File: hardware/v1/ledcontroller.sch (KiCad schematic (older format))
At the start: 4 parts, among them U1 MAX7221

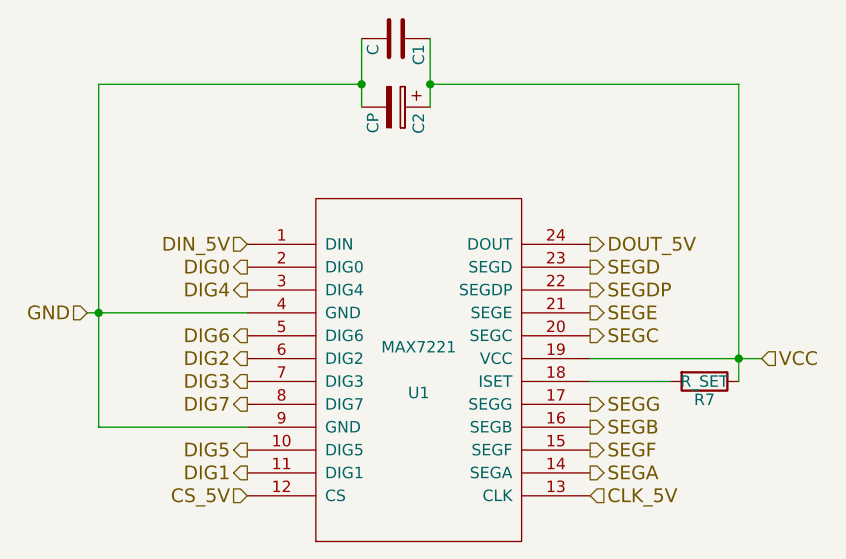
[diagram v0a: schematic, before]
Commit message: Some autorouting on 16led row
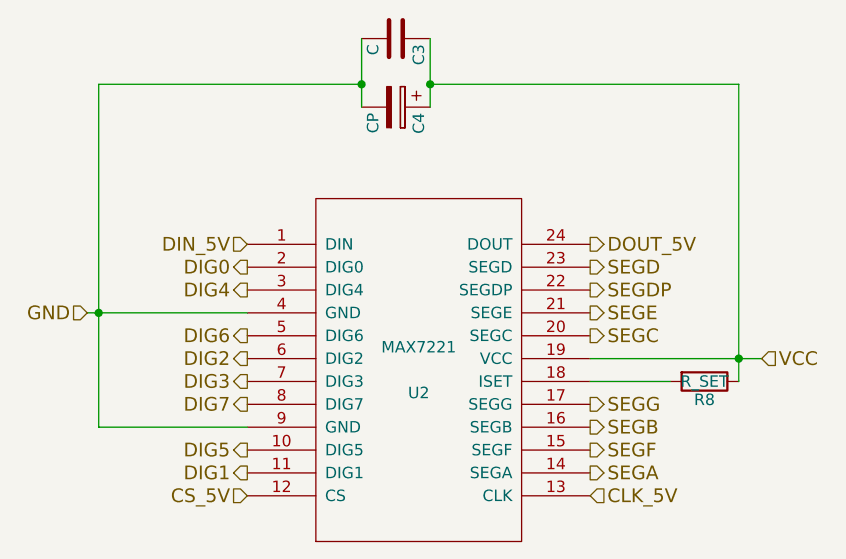
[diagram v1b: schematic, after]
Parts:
- C2: footprint Discret:CP4 -> Discret:CP36V
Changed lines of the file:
@@
 U 1 1 57A34228
 P 5750 3600
-F 0 "U1" H 5750 3500 50  0000 C CNN
+AR Path="/57A2FF40/57A5CF2B/57A34228" Ref="U1"  Part="1"
+AR Path="/57A2FF40/57A5D8B0/57A34228" Ref="U2"  Part="1"
+AR Path="/57A30207/57A34228" Ref="U4"  Part="1"
+F 0 "U2" H 5750 3500 50  0000 C CNN
 F 1 "MAX7221" H 5750 3700 50  0000 C CNN
 F 2 "DIL24:DIL24" H 5750 3600 50  0001 C CNN
@@
 U 1 1 57A343D9
 P 7000 3650
-F 0 "R7" V 7080 3650 50  0000 C CNN
+AR Path="/57A2FF40/57A5CF2B/57A343D9" Ref="R7"  Part="1"
+AR Path="/57A2FF40/57A5D8B0/57A343D9" Ref="R8"  Part="1"
+AR Path="/57A30207/57A343D9" Ref="R9"  Part="1"
+F 0 "R8" V 7080 3650 50  0000 C CNN
 F 1 "R_SET" V 7000 3650 50  0000 C CNN
 F 2 "Resistors_ThroughHole:Resistor_Horizontal_RM10mm" V 6930 3650 50  0001 C CNN
@@
 U 1 1 57A3585E
 P 5650 2150
-F 0 "C1" H 5675 2250 50  0000 L CNN
+AR Path="/57A2FF40/57A5CF2B/57A3585E" Ref="C1"  Part="1"
+AR Path="/57A2FF40/57A5D8B0/57A3585E" Ref="C3"  Part="1"
+AR Path="/57A30207/57A3585E" Ref="C5"  Part="1"
+F 0 "C3" H 5675 2250 50  0000 L CNN
 F 1 "C" H 5675 2050 50  0000 L CNN
 F 2 "Capacitors_ThroughHole:C_Disc_D6_P5" H 5688 2000 50  0001 C CNN
@@
 U 1 1 57A358C3
 P 5650 2450
-F 0 "C2" H 5675 2550 50  0000 L CNN
+AR Path="/57A2FF40/57A5CF2B/57A358C3" Ref="C2"  Part="1"
+AR Path="/57A2FF40/57A5D8B0/57A358C3" Ref="C4"  Part="1"
+AR Path="/57A30207/57A358C3" Ref="C6"  Part="1"
+F 0 "C4" H 5675 2550 50  0000 L CNN
 F 1 "CP" H 5675 2350 50  0000 L CNN
-F 2 "Discret:CP4" H 5688 2300 50  0001 C CNN
+F 2 "Discret:CP36V" H 5688 2300 50  0001 C CNN
 F 3 "" H 5650 2450 50  0000 C CNN
 	1    5650 2450
